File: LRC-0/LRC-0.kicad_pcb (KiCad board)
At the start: 4 copper layers, 100 x 100 mm, 57 parts, among them J1 USB_C_Receptacle_USB2.0_14P, J2 Battery, J3 Conn_01x10, J4 SMA, J5 u.FL, SW1 EN, SW2 BOOT, U1 AP7361C-33E, U2 TVS1400DRV, U3 BQ24075RGT, U4 ESP32-C6-MINI-1, U5 SX1262IMLTRT, U6 4259-63, U8 4259-63, Y1 TX32-33015S-32.000-X-R

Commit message: repositioning
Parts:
- moved C17 19.2 mm to (43.2, 15.2)
- moved U6 19.2 mm to (41.6, 38.2), turned to 90 degrees
- moved C26 19.2 mm to (39.4, 37.4), turned to 180 degrees
- moved C12 17.9 mm to (57.9, 6.22)
- moved FB1 15.6 mm to (54.5, 4.52)
- moved R14 15.1 mm to (57.9, 8.20)
- moved L2 14.8 mm to (54.5, 7.03)
- moved C11 13.7 mm to (57.9, 4.25)
- moved C22 9.18 mm to (41.6, 30.6), turned to 90 degrees
- moved Y1 6.51 mm to (56.5, 18.6)
- moved C25 6.39 mm to (43.4, 29.3), turned to -90 degrees
- moved U8 6.30 mm to (41.6, 28.0), turned to -90 degrees
- moved C13 2.46 mm to (44.6, 20.8)
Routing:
- net Net-(U8-CTRL): track 29.4 -> 15.5 mm
- net /RF1: track 9.08 -> 2.48 mm
- net /RF2: track 7.26 -> 2.48 mm
- net Net-(Y1-VDC): track 4.76 -> 0.00 mm
- net +3V3: track 14.5 -> 11.2 mm, vias 7 -> 5
- net Net-(U5-VREG): track 1.53 -> 3.67 mm
- net Net-(U5-DCC_SW): track 1.53 -> 3.43 mm
- net Net-(Y1-OUTPUT): track 1.58 -> 0.00 mm
- net /XTA: track 1.41 -> 0.00 mm
- net /DIO3: track 1.41 -> 0.00 mm
- net Net-(C12-Pad1): track 1.04 -> 0.00 mm

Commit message: first pass done
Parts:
- L2: footprint Inductor_SMD:L_0603_1608Metric -> Inductor_SMD:L_1008_2520Metric
- moved H1 139.6 mm to (119.2, 77.6)
- moved H2 139.6 mm to (119.2, 83.5)
- moved H3 139.6 mm to (119.2, 89.5)
- moved H4 139.6 mm to (119.2, 95.5)
- moved J3 139.6 mm to (113.9, 64.7)
- moved J4 61.0 mm to (34.9, 40.5), turned to -90 degrees
- moved J5 54.3 mm to (42.2, 35.4)
- moved C7 43.1 mm to (11.8, 35.3), turned to 90 degrees
- moved C6 42.3 mm to (10.8, 35.3), turned to 90 degrees
- moved R5 41.6 mm to (9.38, 34.4)
- moved C4 41.6 mm to (7.86, 33.1)
- moved D1 41.6 mm to (11.3, 38.4)
- moved D2 41.6 mm to (11.3, 40.6)
- moved R10 41.6 mm to (14.1, 38.4)
- moved R4 41.6 mm to (6.38, 31.6)
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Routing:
- net /ANT_CTRL: track 1.50 -> 32.9 mm, vias 1 -> 2
- net /BUSY: track 15.7 -> 8.02 mm
- net /SCK: track 15.5 -> 7.86 mm
- net /MISO: track 15.8 -> 8.10 mm
- net /DIO1: track 15.8 -> 8.15 mm
- net /MOSI: track 15.6 -> 7.98 mm
- net +3V3: track 11.2 -> 18.2 mm, vias 5 -> 7
- net Net-(Y1-VDC): track 0.00 -> 6.09 mm
- net GND: track 22.1 -> 27.4 mm, vias 51 -> 54
- net /ANT2: track 0.00 -> 5.12 mm
- net Net-(Y1-OUTPUT): track 0.00 -> 5.02 mm
- net /NRESET: track 18.3 -> 13.7 mm
- net /NSS: track 21.6 -> 16.9 mm
- net /ANT1: track 0.00 -> 4.52 mm
- net VCC: track 5.72 -> 1.93 mm, vias 0 -> 1
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- added copper zone on F.Cu, net /BAT+
- added copper zone on F.Cu, net VCC
- removed copper zone on F.Cu, net +3V3
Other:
- board size 100 x 100 mm -> 50 x 38.5 mm

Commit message: DRC fixes
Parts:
- turned U3 to 0 degrees
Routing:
- net GND: track 27.4 -> 34.7 mm, vias 54 -> 59
- net VCC: track 1.93 -> 0.00 mm, vias 1 -> 0
- net Net-(U3-ISET): track 3.63 -> 2.95 mm, vias 1 -> 0
- net +3V3: track 18.2 -> 18.9 mm, vias 7 -> 9
- added copper zone on F.Cu, net +3V3

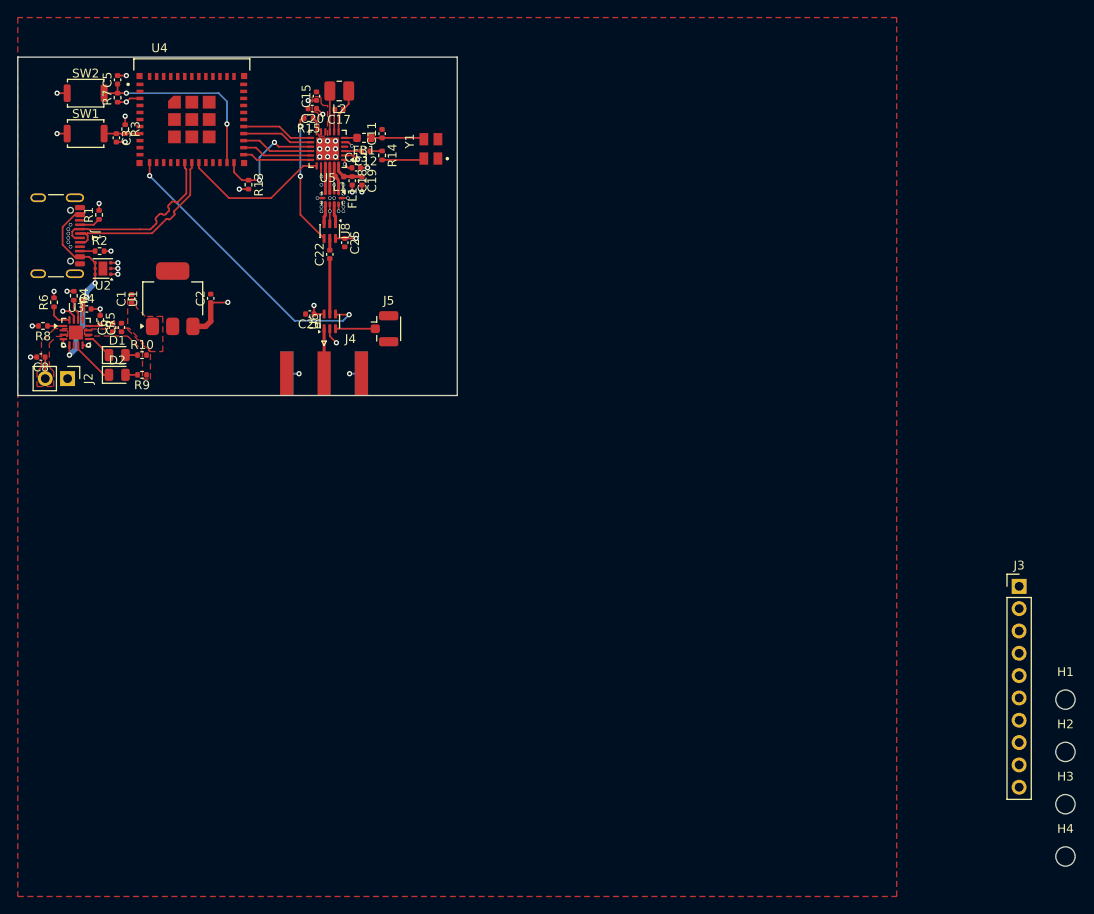
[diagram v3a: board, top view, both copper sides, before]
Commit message: charging circuit reposition
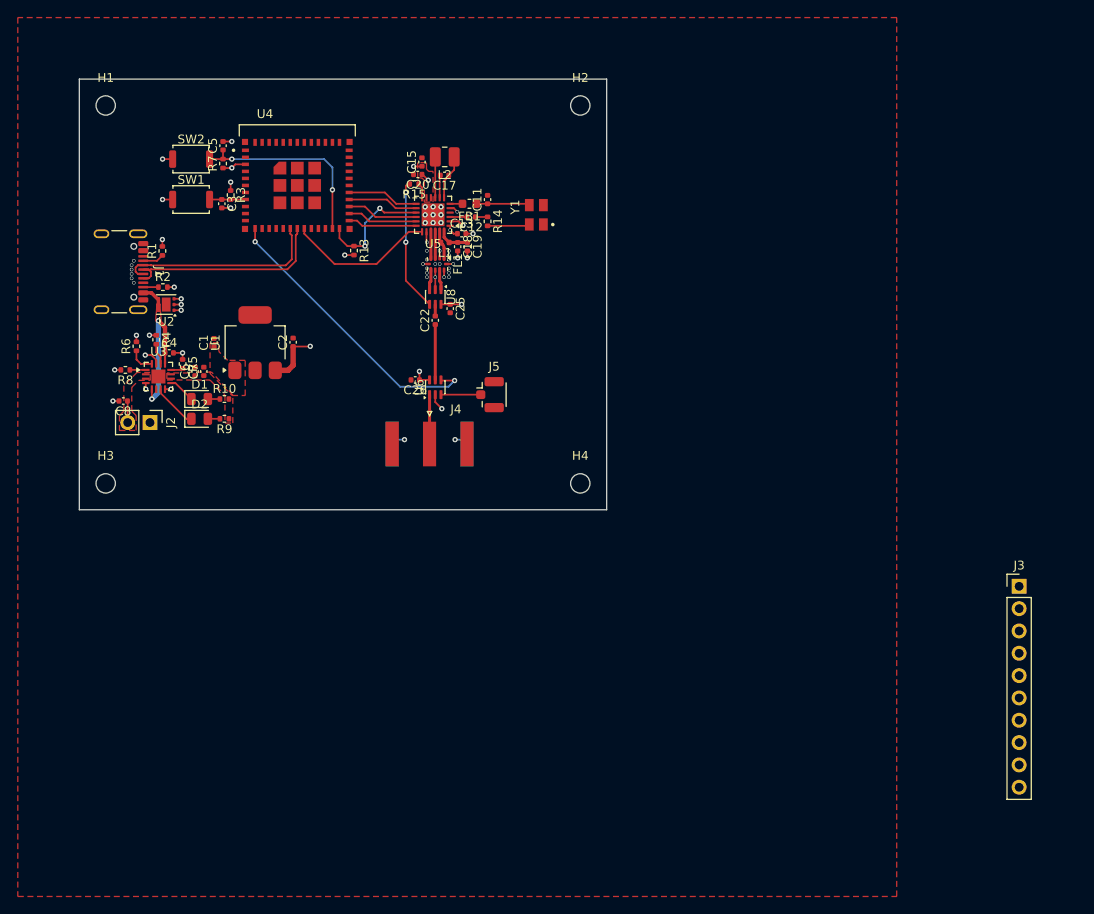
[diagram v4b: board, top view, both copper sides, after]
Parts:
- moved H1 128.4 mm to (10.0, 10.0)
- moved H3 115.1 mm to (10.0, 53.0)
- moved H2 92.0 mm to (64.0, 10.0)
- moved H4 69.6 mm to (64.0, 53.0)
- moved J4 14.4 mm to (46.9, 48.5)
- moved C5 14.2 mm to (23.4, 14.6)
- moved R7 14.2 mm to (23.4, 16.6)
- moved SW2 14.2 mm to (19.7, 16.1)
- moved U4 14.2 mm to (31.8, 19.1)
- moved C11 14.2 mm to (53.5, 20.7)
- moved C12 14.2 mm to (51.6, 22.7)
- moved C13 14.2 mm to (50.5, 24.6)
- moved C15 14.2 mm to (46.0, 16.4)
- moved C17 14.2 mm to (48.5, 18.0)
- moved C18 14.2 mm to (50.0, 26.1)
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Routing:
- net +5V: track 24.8 -> 18.7 mm, vias 3 -> 2
- net /D+: track 20.9 -> 24.0 mm
- net /D-: track 20.9 -> 23.2 mm
- added copper zone on F.Cu, net +5V
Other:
- board size 50 x 38.5 mm -> 60 x 49 mm

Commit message: shielding and pd redesign
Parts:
- moved C1 9.90 mm to (15.3, 30.0)
- moved C2 9.90 mm to (24.3, 29.9)
- moved C6 9.90 mm to (13.2, 33.3)
- moved C7 9.90 mm to (14.2, 33.3)
- moved R2 9.90 mm to (9.51, 23.7)
- moved R3 9.90 mm to (17.2, 13.2)
- moved U1 9.90 mm to (20.0, 30.0)
- moved U4 9.90 mm to (24.8, 12.1)
- moved C11 9.90 mm to (46.5, 13.7)
- moved C12 9.90 mm to (44.6, 15.7)
- moved C13 9.90 mm to (43.5, 17.6)
- moved C15 9.90 mm to (39.0, 9.44)
- moved C17 9.90 mm to (41.5, 11.0)
- moved C18 9.90 mm to (43.0, 19.1)
- moved C19 9.90 mm to (44.1, 19.1)
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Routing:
- net /ANT2: track 5.12 -> 10.6 mm
- net GND: track 34.7 -> 32.0 mm, vias 59 -> 381

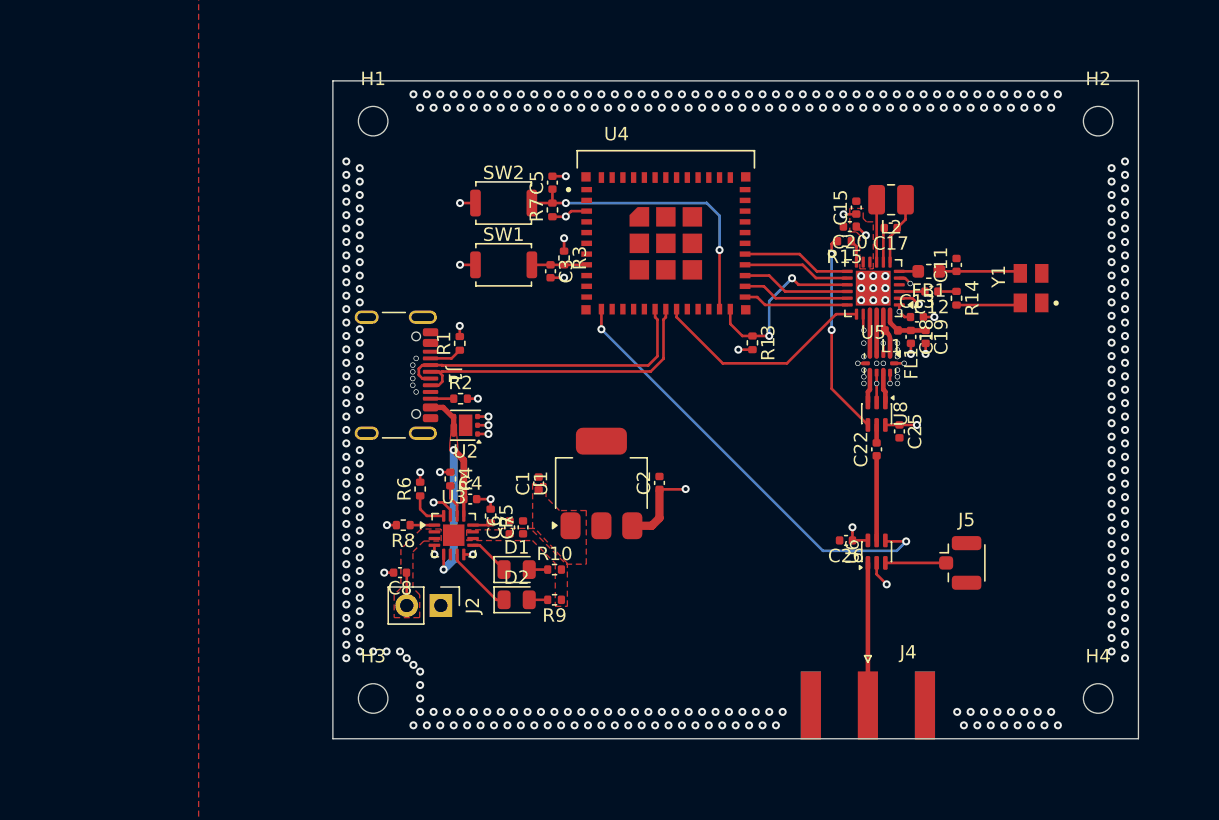
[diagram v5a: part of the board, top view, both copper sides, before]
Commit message: more shielding and LDO/power redesign + on/off switch
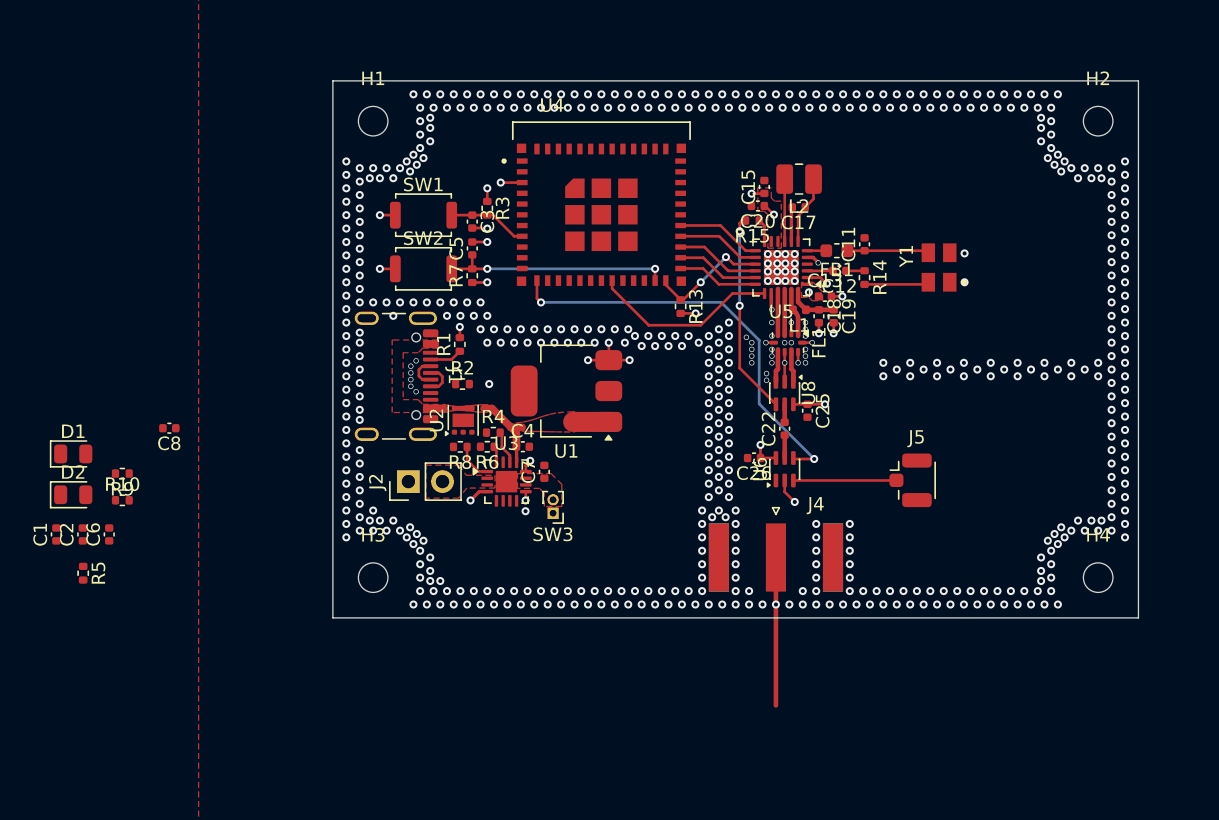
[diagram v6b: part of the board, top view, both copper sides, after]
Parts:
- added SW3: SW_SPDT, Connector_PinHeader_1.00mm:PinHeader_1x02_P1.00mm_Vertical, F.Cu at (16.4, 32.2)
- moved C2 43.1 mm to (-18.6, 33.8)
- moved C1 36.1 mm to (-20.6, 33.8)
- moved D1 34.1 mm to (-19.3, 27.8)
- moved D2 33.9 mm to (-19.3, 30.8)
- moved R9 33.5 mm to (-15.7, 29.2)
- moved R10 32.6 mm to (-15.7, 31.2)
- moved R5 30.6 mm to (-18.6, 36.7)
- moved C6 29.8 mm to (-16.7, 33.8)
- moved C8 20.3 mm to (-12.2, 25.9)
- moved J4 13.0 mm to (33.0, 35.5)
- moved J2 9.54 mm to (5.62, 29.8), turned to 90 degrees
- moved U6 9.20 mm to (33.6, 28.9)
- moved C26 9.20 mm to (31.4, 28.1)
- moved H3 9.00 mm to (3.00, 37.0)
- moved H4 9.00 mm to (57.0, 37.0)
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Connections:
- C1 pad 1: VCC -> VBUS
- C4 pad 1: +5V -> VBUS
- C6 pad 1: VCC -> VOUT
- C7 pad 1: VCC -> VOUT
- J1 pad A4: +5V -> VBUS
- J1 pad A9: +5V -> VBUS
- J1 pad B4: +5V -> VBUS
- J1 pad B9: +5V -> VBUS
- R10 pad 2: VCC -> VOUT
- R9 pad 1: VCC -> VOUT
- U1 pad 1: VCC -> VBUS
- U2 pad 4: +5V -> VBUS
- U2 pad 5: +5V -> VBUS
- U2 pad 6: +5V -> VBUS
- U3 pad 10: VCC -> VOUT
- U3 pad 11: VCC -> VOUT
- U3 pad 13: +5V -> VBUS
- U3 pad 5: +5V -> VCC
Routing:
- net /D+: track 24.0 -> 2.44 mm
- net /D-: track 23.2 -> 2.44 mm
- net +5V: track 18.7 -> 0.00 mm, vias 2 -> 0
- net VBUS: track 0.00 -> 11.1 mm
- net GND: track 32.0 -> 22.6 mm, vias 381 -> 571
- net Net-(U4-IO9): track 22.4 -> 17.1 mm
- net Net-(D2-K): track 5.16 -> 0.00 mm
- net /NRESET: track 13.7 -> 8.98 mm
- net /RFIN_A: track 6.30 -> 1.69 mm
- net +3V3: track 18.9 -> 15.6 mm, vias 9 -> 12
- net /ANT1: track 4.52 -> 7.68 mm
- net /NSS: track 16.9 -> 14.1 mm
- net Net-(D1-K): track 3.06 -> 0.66 mm, vias 0 -> 1
- net /BAT+: track 2.27 -> 0.00 mm
- net /BUSY: track 8.02 -> 6.22 mm
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- added copper zone on F.Cu, net VBUS
- added copper zone on F.Cu, net VOUT
- removed copper zone on F.Cu, net +5V
- removed copper zone on F.Cu, net VCC
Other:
- board size 60 x 49 mm -> 60 x 40 mm

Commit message: stitching
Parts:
- moved J3 82.6 mm to (34.8, 41.2), turned to -90 degrees
- moved H2 63.8 mm to (3.00, 37.0), turned to 180 degrees
- moved H4 63.8 mm to (3.00, 3.00), turned to 180 degrees
- moved D2 59.7 mm to (34.0, 4.10), turned to -90 degrees
- moved C6 55.4 mm to (32.1, 7.50), turned to 0 degrees
- moved D1 54.6 mm to (30.0, 4.31), turned to -90 degrees
- moved R9 54.2 mm to (33.5, 6.39), turned to 0 degrees
- moved R5 54.0 mm to (29.8, 12.8), turned to 0 degrees
- moved R10 53.7 mm to (31.6, 5.76), turned to -90 degrees
- moved C8 53.4 mm to (37.8, 7.27), turned to 90 degrees
- moved H1 52.5 mm to (43.0, 37.0), turned to 180 degrees
- moved H3 52.5 mm to (43.0, 3.00), turned to 180 degrees
- moved J5 43.8 mm to (4.25, 10.2), turned to 180 degrees
- moved C1 43.5 mm to (19.0, 15.7), turned to -90 degrees
- moved Y1 42.7 mm to (4.25, 26.1), turned to -90 degrees
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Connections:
- net GND renamed Earth_Protective
- C1 pad 1: VBUS -> VCC
- U1 pad 1: VBUS -> VCC
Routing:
- net VCC: track 0.00 -> 19.6 mm, vias 0 -> 2
- net /D+: track 2.44 -> 19.7 mm
- net /D-: track 2.44 -> 18.9 mm
- net Net-(D2-K): track 0.00 -> 7.20 mm
- net /ANT2: track 10.6 -> 5.73 mm
- net VBUS: track 11.1 -> 7.62 mm
- net Net-(Y1-OUTPUT): track 5.02 -> 1.62 mm
- net Net-(Y1-VDC): track 6.09 -> 2.69 mm
- net /BAT+: track 0.00 -> 2.41 mm
- net /ANT1: track 7.68 -> 5.48 mm
- net +3V3: track 15.6 -> 17.8 mm
- net Earth_Protective: track 22.6 -> 20.7 mm, vias 571 -> 678
- net Net-(D1-A): track 0.00 -> 1.60 mm
- net Net-(U3-ILIM): track 0.93 -> 2.41 mm, vias 1 -> 0
- net Net-(U5-VREG): track 5.12 -> 3.84 mm
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- added copper zone on F.Cu, net /ANT1
- added copper zone on B.Cu, net Earth_Protective
- added copper zone on F.Cu, net VCC
- removed copper zone on F.Cu, net VOUT
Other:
- board size 60 x 40 mm -> 46 x 40 mm

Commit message: bom and jlcpcb quote
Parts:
- removed J3: Conn_01x10, Connector_PinHeader_2.54mm:PinHeader_1x10_P2.54mm_Vertical
- H1, H2, H3, H4: value MountingHole -> MountingHole_Pad_MP; footprint MountingHole:MountingHole_2.2mm_M2 -> MountingHole:MountingHole_2.2mm_M2_Pad_TopOnly
- moved H1 52.5 mm to (3.00, 3.00), turned to 0 degrees
- moved H4 52.5 mm to (43.0, 37.0), turned to 0 degrees
- turned H2 to 0 degrees
- turned H3 to 0 degrees
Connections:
- C11 pad 2: Earth_Protective -> unconnected-(C11-Pad2)
- Y1 pad 1: Earth_Protective -> Net-(Y1-GND)
- Y1 pad 2: Earth_Protective -> Net-(Y1-GND)
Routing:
- net Net-(D1-K): track 0.00 -> 7.53 mm
- net Earth_Protective: vias 678 -> 725
